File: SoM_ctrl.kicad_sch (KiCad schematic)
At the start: 19 parts, among them J2 Hermaphroditic_Molex_203456-0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

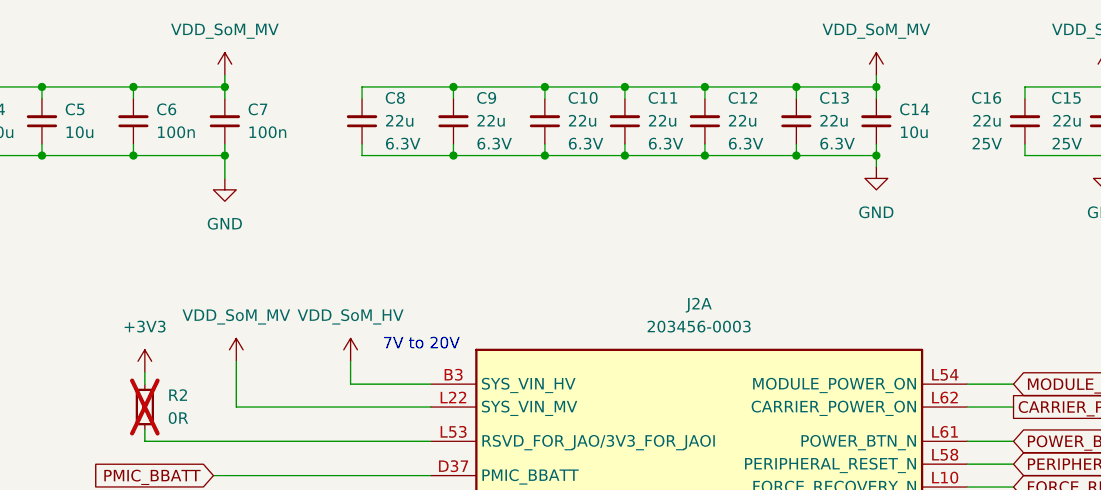
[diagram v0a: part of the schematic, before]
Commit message: [#81778] Rename power label
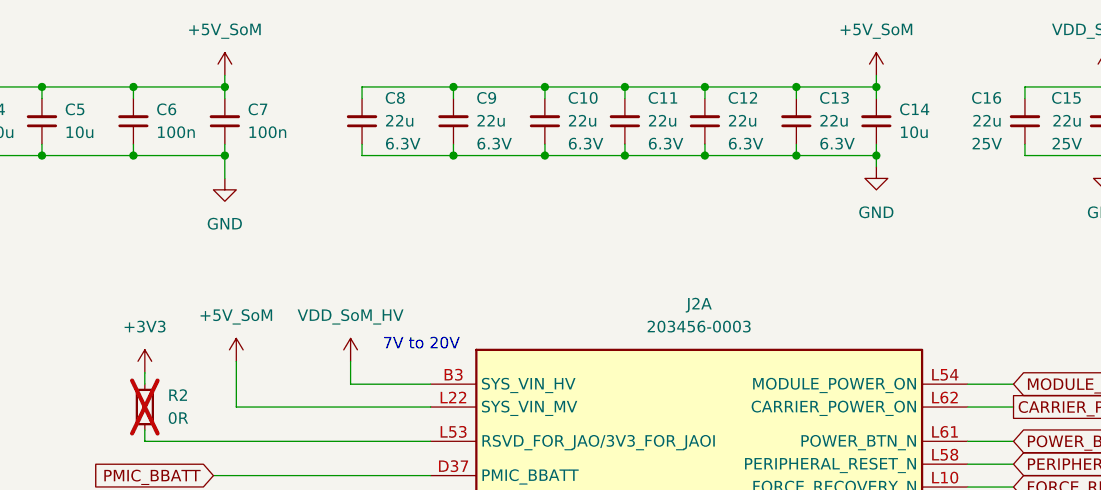
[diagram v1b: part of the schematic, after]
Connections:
- net SYS_VIN_MV renamed +5V_SoM
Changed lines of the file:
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@@
 			)
 		)
-		(property "Value" "VDD_SoM_MV"
+		(property "Value" "+5V_SoM"
 			(at 78.74 54.61 0)
 			(effects
@@
 	(symbol
 		(lib_id "antmicropower:+5V")
-		(at 149.86 27.94 0)
+		(at 77.47 27.94 0)
 		(unit 1)
 		(exclude_from_sim no)
@@
 		(dnp no)
 		(fields_autoplaced yes)
-		(property "Reference" "#PWR06"
-			(at 165.1 30.48 0)
-			(effects
-				(font
-					(size 1.27 1.27)
-					(thickness 0.15)
-				)
-				(justify left bottom)
-				(hide yes)
-			)
-		)
-		(property "Value" "VDD_SoM_MV"
-			(at 149.86 22.86 0)
+		(property "Reference" "#PWR012"
+			(at 92.71 30.48 0)
+			(effects
+				(font
+					(size 1.27 1.27)
+					(thickness 0.15)
+				)
+				(justify left bottom)
+				(hide yes)
+			)
+		)
+		(property "Value" "+5V_SoM"
+			(at 77.47 22.86 0)
 			(effects
 				(font
@@
 		)
 		(property "Footprint" ""
-			(at 165.1 35.56 0)
+			(at 92.71 35.56 0)
 			(effects
 				(font
@@
 		)
 		(property "Datasheet" ""
-			(at 165.1 38.1 0)
+			(at 92.71 38.1 0)
 			(effects
 				(font
@@
 		)
 		(property "Description" ""
-			(at 149.86 27.94 0)
+			(at 77.47 27.94 0)
 			(effects
 				(font
@@
 		)
 		(property "Author" "Antmicro"
-			(at 165.1 35.56 0)
+			(at 92.71 35.56 0)
 			(effects
 				(font
@@
 		)
 		(property "License" "Apache-2.0"
-			(at 165.1 38.1 0)
+			(at 92.71 38.1 0)
 			(effects
 				(font
@@
 			(project "jetson-orin-agx-baseboard"
 				(path "/f569b0be-0afd-48b7-93ee-28582a4c645c/4579c4a7-22a6-485d-a5cb-a4d2e4f367db/ee8699d0-a5ca-448c-bd2c-e78e8401ec10"
-					(reference "#PWR06")
+					(reference "#PWR012")
 					(unit 1)
 				)
@@
 	)
 	(symbol
-		(lib_id "antmicropower:+5V")
-		(at 77.47 27.94 0)
-		(unit 1)
-		(exclude_from_sim no)
-		(in_bom yes)
-		(on_board yes)
-		(dnp no)
-		(fields_autoplaced yes)
-		(property "Reference" "#PWR04"
-			(at 92.71 30.48 0)
-			(effects
-				(font
-					(size 1.27 1.27)
-					(thickness 0.15)
-				)
-				(justify left bottom)
-				(hide yes)
-			)
-		)
-		(property "Value" "VDD_SoM_MV"
-			(at 77.47 22.86 0)
-			(effects
-				(font
-					(size 1.27 1.27)
-					(thickness 0.15)
-				)
-			)
-		)
-		(property "Footprint" ""
-			(at 92.71 35.56 0)
-			(effects
-				(font
-					(size 1.27 1.27)
-					(thickness 0.15)
-				)
-				(justify left bottom)
-				(hide yes)
-			)
-		)
-		(property "Datasheet" ""
-			(at 92.71 38.1 0)
-			(effects
-				(font
-					(size 1.27 1.27)
-					(thickness 0.15)
-				)
-				(justify left bottom)
-				(hide yes)
-			)
-		)
-		(property "Description" ""
-			(at 77.47 27.94 0)
-			(effects
-				(font
-					(size 1.27 1.27)
-				)
-				(hide yes)
-			)
-		)
-		(property "Author" "Antmicro"
-			(at 92.71 35.56 0)
-			(effects
-				(font
-					(size 1.27 1.27)
-					(thickness 0.15)
-				)
-				(justify left bottom)
-				(hide yes)
-			)
-		)
-		(property "License" "Apache-2.0"
-			(at 92.71 38.1 0)
-			(effects
-				(font
-					(size 1.27 1.27)
-					(thickness 0.15)
-				)
-				(justify left bottom)
-				(hide yes)
-			)
-		)
-		(pin "1"
-		)
-		(instances
-			(project "jetson-orin-agx-baseboard"
-				(path "/f569b0be-0afd-48b7-93ee-28582a4c645c/4579c4a7-22a6-485d-a5cb-a4d2e4f367db/ee8699d0-a5ca-448c-bd2c-e78e8401ec10"
-					(reference "#PWR04")
-					(unit 1)
-				)
-			)
-		)
-	)
-	(symbol
 		(lib_id "antmicroCapacitorsmisc:C_22u_6.3V_X7R_0805")
 		(at 102.87 35.56 90)
@@
 					(unit 1)
 				)
+			)
+		)
+	)
+	(symbol
+		(lib_id "antmicropower:+5V")
+		(at 149.86 27.94 0)
+		(unit 1)
+		(exclude_from_sim no)
+		(in_bom yes)
+		(on_board yes)
+		(dnp no)
+		(fields_autoplaced yes)
+		(property "Reference" "#PWR04"
+			(at 165.1 30.48 0)
+			(effects
+				(font
+					(size 1.27 1.27)
+					(thickness 0.15)
+				)
+				(justify left bottom)
+				(hide yes)
+			)
+		)
+		(property "Value" "+5V_SoM"
+			(at 149.86 22.86 0)
+			(effects
+				(font
+					(size 1.27 1.27)
+					(thickness 0.15)
+				)
+			)
+		)
+		(property "Footprint" ""
+			(at 165.1 35.56 0)
+			(effects
+				(font
+					(size 1.27 1.27)
+					(thickness 0.15)
+				)
+				(justify left bottom)
+				(hide yes)
+			)
+		)
+		(property "Datasheet" ""
+			(at 165.1 38.1 0)
+			(effects
+				(font
+					(size 1.27 1.27)
+					(thickness 0.15)
+				)
+				(justify left bottom)
+				(hide yes)
+			)
+		)
+		(property "Description" ""
+			(at 149.86 27.94 0)
+			(effects
+				(font
+					(size 1.27 1.27)
+				)
+				(hide yes)
+			)
+		)
+		(property "Author" "Antmicro"
+			(at 165.1 35.56 0)
+			(effects
+				(font
+					(size 1.27 1.27)
+					(thickness 0.15)
+				)
+				(justify left bottom)
+				(hide yes)
+			)
+		)
+		(property "License" "Apache-2.0"
+			(at 165.1 38.1 0)
+			(effects
+				(font
+					(size 1.27 1.27)
+					(thickness 0.15)
+				)
+				(justify left bottom)
+				(hide yes)
+			)
+		)
+		(pin "1"
+		)
+		(instances
+			(project "jetson-orin-agx-baseboard"
+				(path "/f569b0be-0afd-48b7-93ee-28582a4c645c/4579c4a7-22a6-485d-a5cb-a4d2e4f367db/ee8699d0-a5ca-448c-bd2c-e78e8401ec10"
+					(reference "#PWR04")
+					(unit 1)
+				)

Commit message: [#81970] Refactor root
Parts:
- renumbered C1 to C17, C2 to C18, C3 to C19, C4 to C20, C5 to C21, C6 to C22, C7 to C23, C8 to C24, C9 to C25, C10 to C26, C11 to C27, C12 to C28, C13 to C29, C14 to C30, C16 to C31, C15 to C32, J2 to J1, R2 to R3, R1 to R4
